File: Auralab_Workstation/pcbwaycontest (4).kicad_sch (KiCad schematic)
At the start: 14 parts, among them J1 Conn_Coaxial, J2 TEST_SOCKET, Q1 BS170, SW1 SW_SPDT, U1 TL072, U2 MCP3201, U3 REF3033, U4 INA226

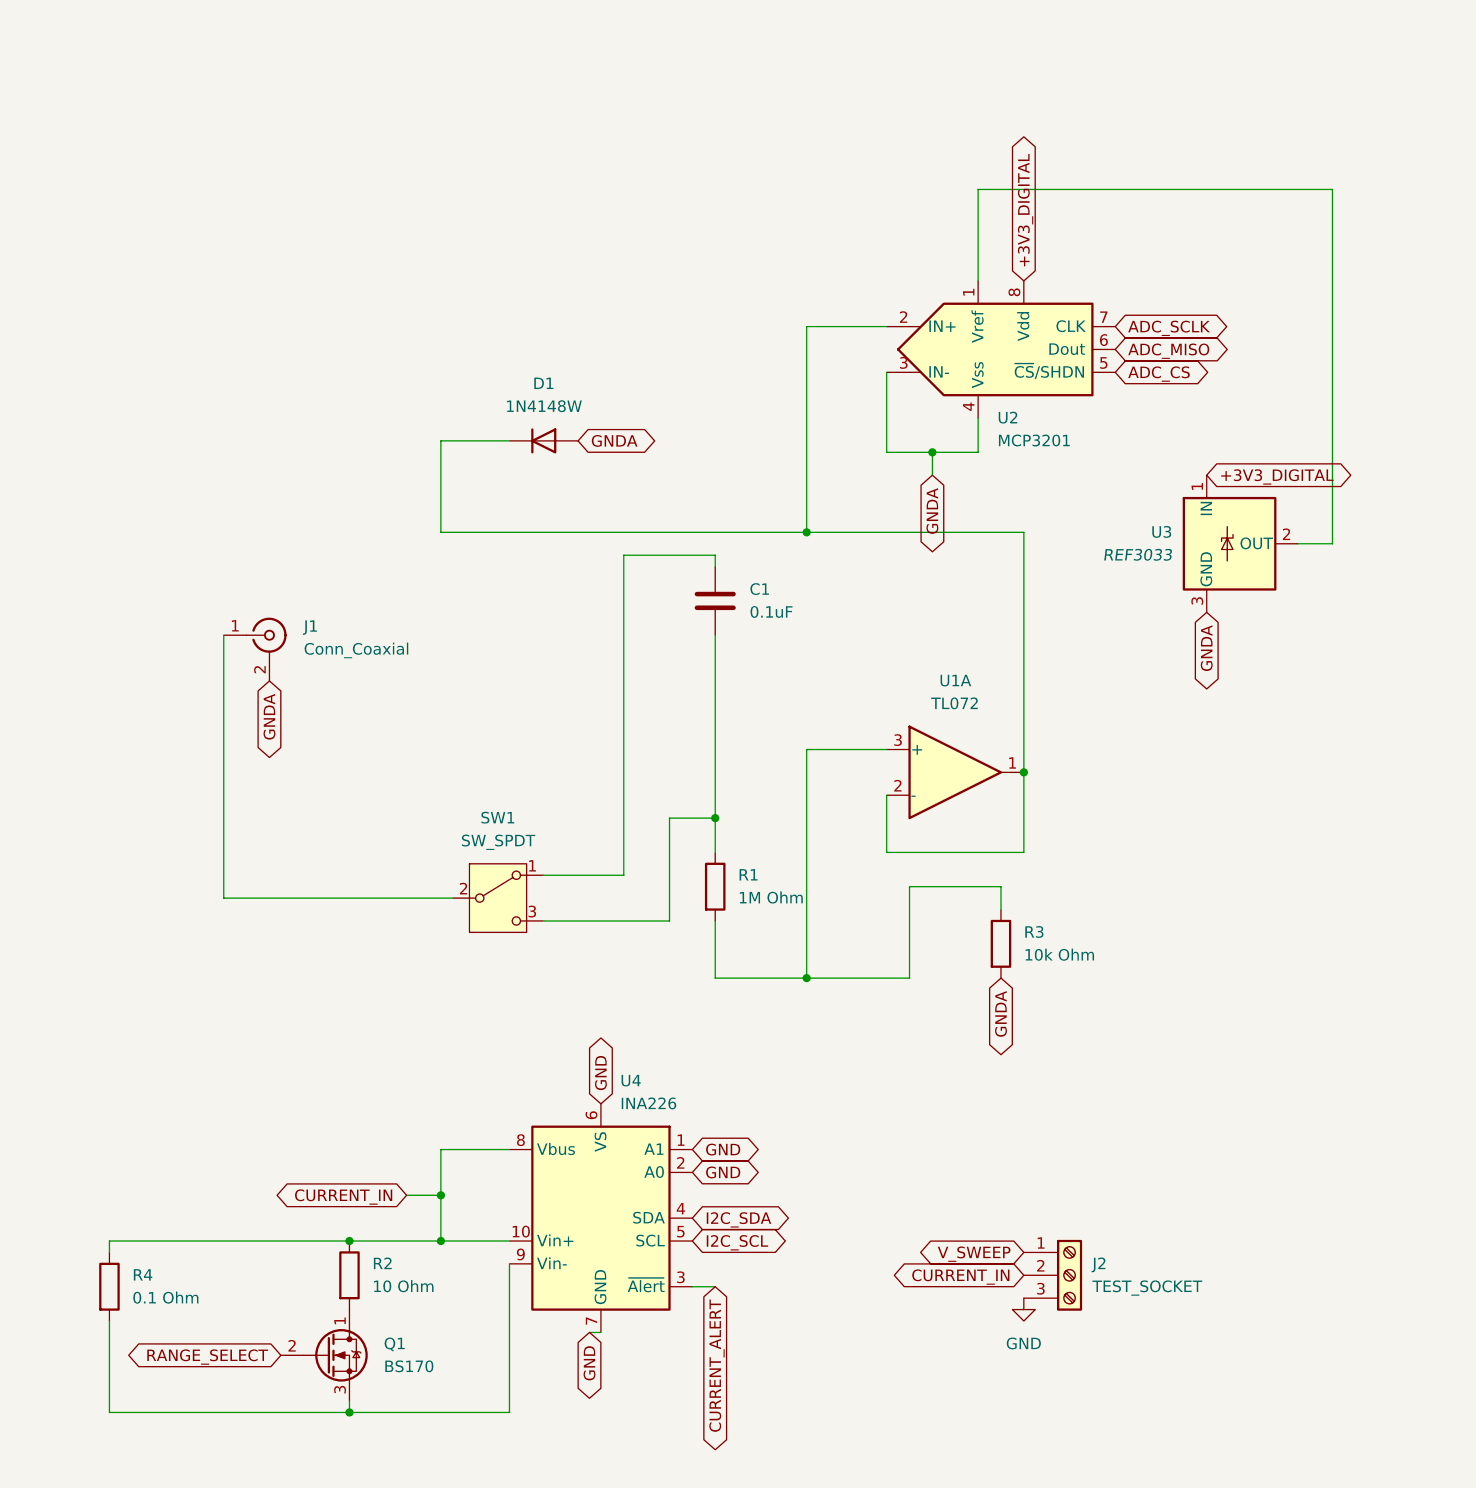
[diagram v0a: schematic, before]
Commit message: Updated gnd, gnda in analog_frontend
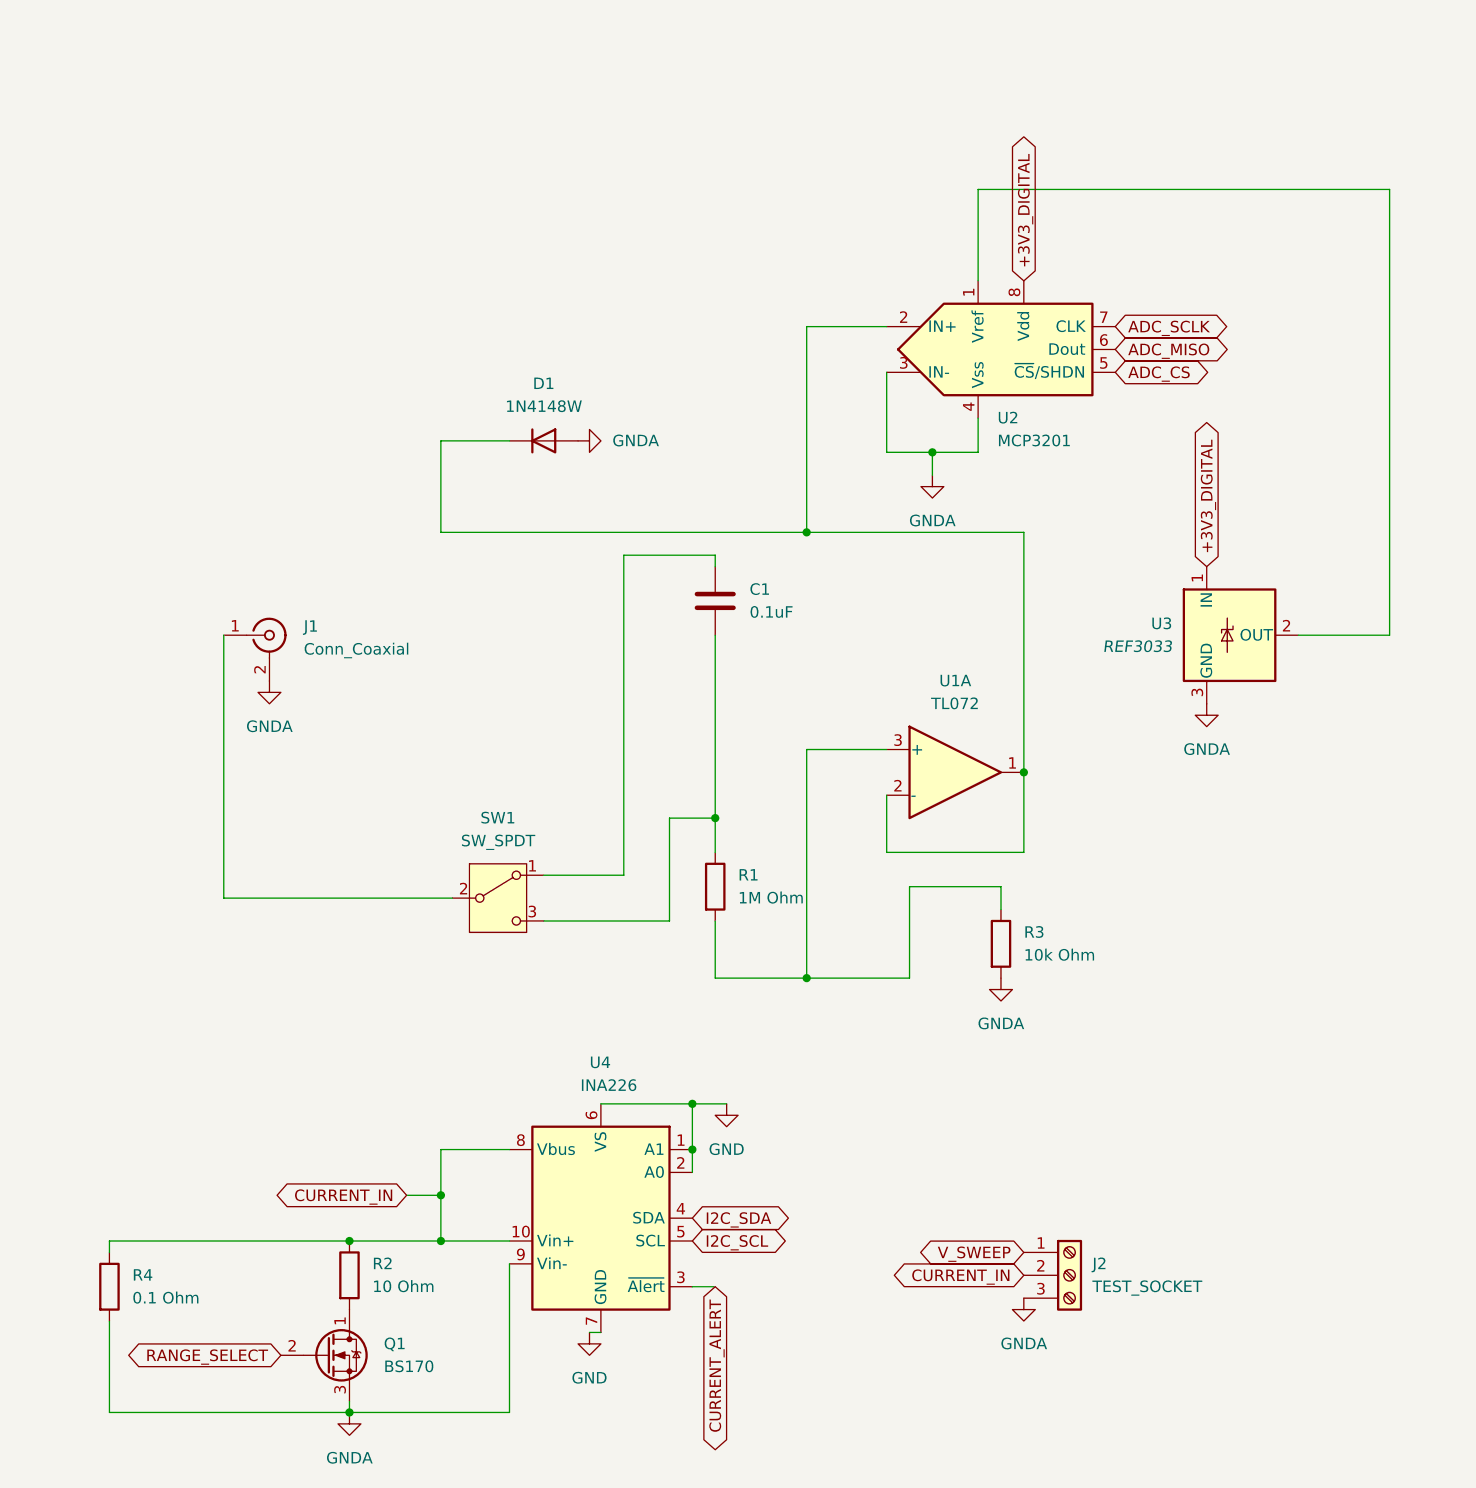
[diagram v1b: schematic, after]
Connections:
- net GND: no longer J2.3 (Pin_3)
- net GNDA: now also J2.3 (Pin_3), Q1.3 (S), R4.2, U4.9 (Vin-)
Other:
- moved on the sheet: U3

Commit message: Check analog part
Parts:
- added C2: 0.1uF, Capacitor_SMD:C_0805_2012Metric, symbol Device:C
- added R5: 10k Ohm, Resistor_SMD:R_0805_2012Metric, symbol Device:R
- added R6: 3.3k Ohm, Resistor_SMD:R_0805_2012Metric, symbol Device:R
- added unit 2 of U1
- added unit 3 of U1
- added U5: TL072, Package_SO:SOIC-8_3.9x4.9mm_P1.27mm, symbol Amplifier_Operational:TL072
- R2: value 10 Ohm -> 0.1 Ohm
- R4: value 0.1 Ohm -> 10 Ohm
- SW1: footprint Connector:FanPinHeader_1x03_P2.54mm_Vertical -> Button_Switch_SMD:SW_SPDT_PCM12
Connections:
- net +3V3_DIGITAL: now also U4.6 (VS), C2.1, U1.8 (V+)
- net GND: now also U2.4 (Vss), C2.2; no longer U4.6 (VS)
- net GNDA: now also R6.2, U1.4 (V-), U1.5 (+), U5.5 (+); no longer U2.4 (Vss)
- net V_SWEEP: now also R5.2, U5.1
- net Vref_ADC: now reaches U2.1 (Vref), U3.2 (OUT)
- net +IN_ADC: now reaches D1.1 (K), U1.1, U1.2 (-), U2.2 (IN+)
- net Non-inv Input OpAmp: now reaches R1.2, R3.1, U1.3 (+)
- new net: R5.1, R6.1, U5.2 (-)
- new net: U5.6 (-), U5.7
- new net: U1.6 (-), U1.7
- new net +Vout: U5.8 (V+)
- new net -Vout: U5.4 (V-)
- new net V_filtered: U5.3 (+)
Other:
- moved on the sheet: C1, D1, J1, J2, Q1, R1, R2, R3, R4, SW1, U1A, U2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
